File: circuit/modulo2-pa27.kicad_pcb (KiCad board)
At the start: 2 copper layers, 105 x 47 mm, 48 parts, among them J1 CONN_01X02, J3 CONN_01X04, J4 JACK_MONO, J5 HOLE, J7 HOLE, SW1 bright, U1 OPA2134, U2 OPA2134, U3 TLE2426, U4 POWER

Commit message: getting closer to the final PCBs; still have to change the rotenc
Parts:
- moved J1 4.00 mm to (85.0, 93.0)
- moved J3 2.00 mm to (74.0, 93.0)
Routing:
- net /PA_OUT: track 30.2 -> 26.0 mm
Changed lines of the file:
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@@
   (net 33 "/MID")
   (footprint "myAmp:PIN_1x04" (layer "F.Cu")
-    (at 76 93)
+    (at 74 93)
     (property "Sheetfile" "modulo2-pa27.kicad_sch")
     (property "Sheetname" "")
@@
   )
   (footprint "myAmp:PIN_1x02" (layer "F.Cu")
-    (at 89 93)
+    (at 85 93)
     (property "Sheetfile" "modulo2-pa27.kicad_sch")
     (property "Sheetname" "")
@@
   (segment (start 89.0524 80.645) (end 90.805 80.645) (width 0.9144) (layer "F.Cu") (net 13))
   (segment (start 82.55 83.185) (end 81.915 83.82) (width 0.9144) (layer "F.Cu") (net 13))
-  (segment (start 90.27 93) (end 90.27 91.54) (width 0.9144) (layer "F.Cu") (net 14))
-  (segment (start 79.81 90.605) (end 79.7306 90.5256) (width 0.9144) (layer "F.Cu") (net 14))
-  (segment (start 77.8764 90.5256) (end 74.6506 90.5256) (width 0.9144) (layer "F.Cu") (net 14))
-  (segment (start 74.73 93) (end 74.73 90.605) (width 0.9144) (layer "F.Cu") (net 14))
-  (segment (start 79.81 93) (end 79.81 90.605) (width 0.9144) (layer "F.Cu") (net 14))
-  (segment (start 79.7306 90.5256) (end 77.8764 90.5256) (width 0.9144) (layer "F.Cu") (net 14))
   (segment (start 70.2056 90.5256) (end 67.945 88.265) (width 0.9144) (layer "F.Cu") (net 14))
-  (segment (start 89.2556 90.5256) (end 79.7306 90.5256) (width 0.9144) (layer "F.Cu") (net 14))
-  (segment (start 74.6506 90.5256) (end 70.2056 90.5256) (width 0.9144) (layer "F.Cu") (net 14))
-  (segment (start 74.73 90.605) (end 74.6506 90.5256) (width 0.9144) (layer "F.Cu") (net 14))
-  (segment (start 90.27 91.54) (end 89.2556 90.5256) (width 0.9144) (layer "F.Cu") (net 14))
+  (segment (start 77.81 90.5412) (end 77.8256 90.5256) (width 0.9144) (layer "F.Cu") (net 14))
+  (segment (start 86.27 93) (end 86.27 91.731) (width 0.9144) (layer "F.Cu") (net 14))
+  (segment (start 72.7456 90.5256) (end 77.8256 90.5256) (width 0.9144) (layer "F.Cu") (net 14))
+  (segment (start 72.73 93) (end 72.73 90.5412) (width 0.9144) (layer "F.Cu") (net 14))
+  (segment (start 77.81 93) (end 77.81 90.5412) (width 0.9144) (layer "F.Cu") (net 14))
+  (segment (start 77.8256 90.5256) (end 85.0646 90.5256) (width 0.9144) (layer "F.Cu") (net 14))
+  (segment (start 86.27 91.731) (end 85.0646 90.5256) (width 0.9144) (layer "F.Cu") (net 14))
+  (segment (start 72.73 90.5412) (end 72.7456 90.5256) (width 0.9144) (layer "F.Cu") (net 14))
+  (segment (start 70.2056 90.5256) (end 72.7456 90.5256) (width 0.9144) (layer "F.Cu") (net 14))
   (segment (start 77.47 58.42) (end 77.47 60.325) (width 0.9144) (layer "F.Cu") (net 15))
   (segment (start 102.87 60.92) (end 107.315 60.92) (width 0.9144) (layer "F.Cu") (net 16))

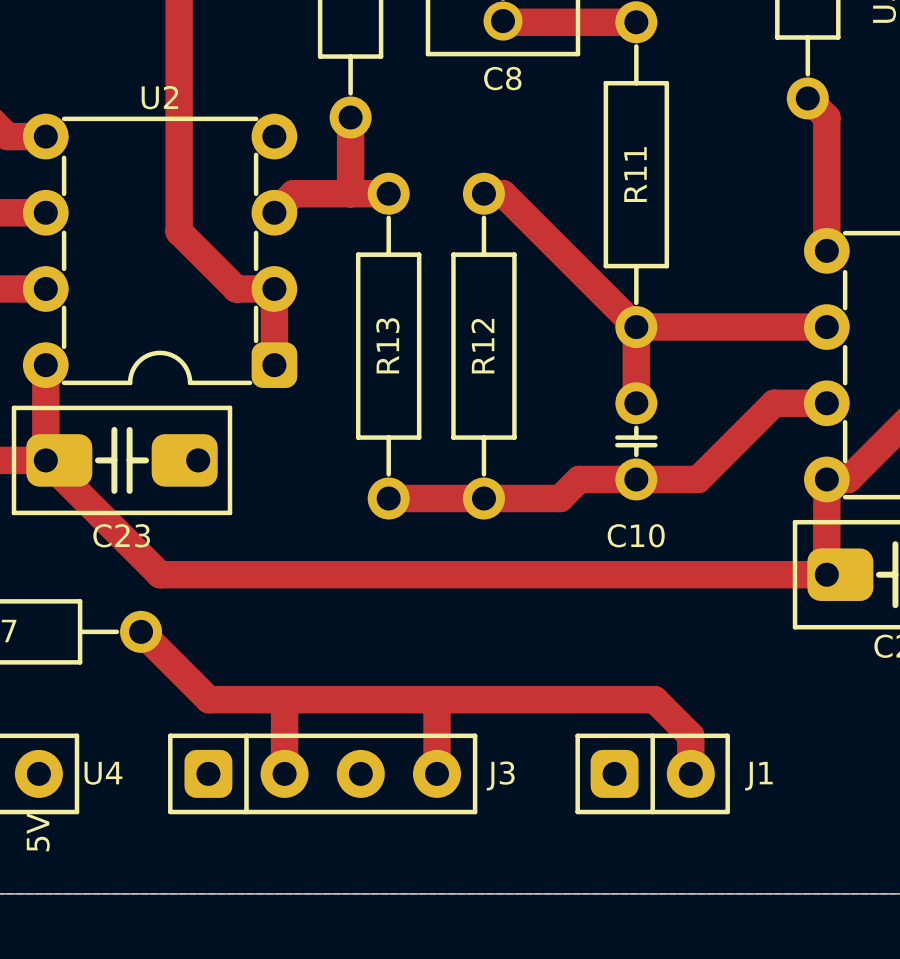
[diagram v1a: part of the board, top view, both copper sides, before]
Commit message: found new switch for gain select; eq needs redesign
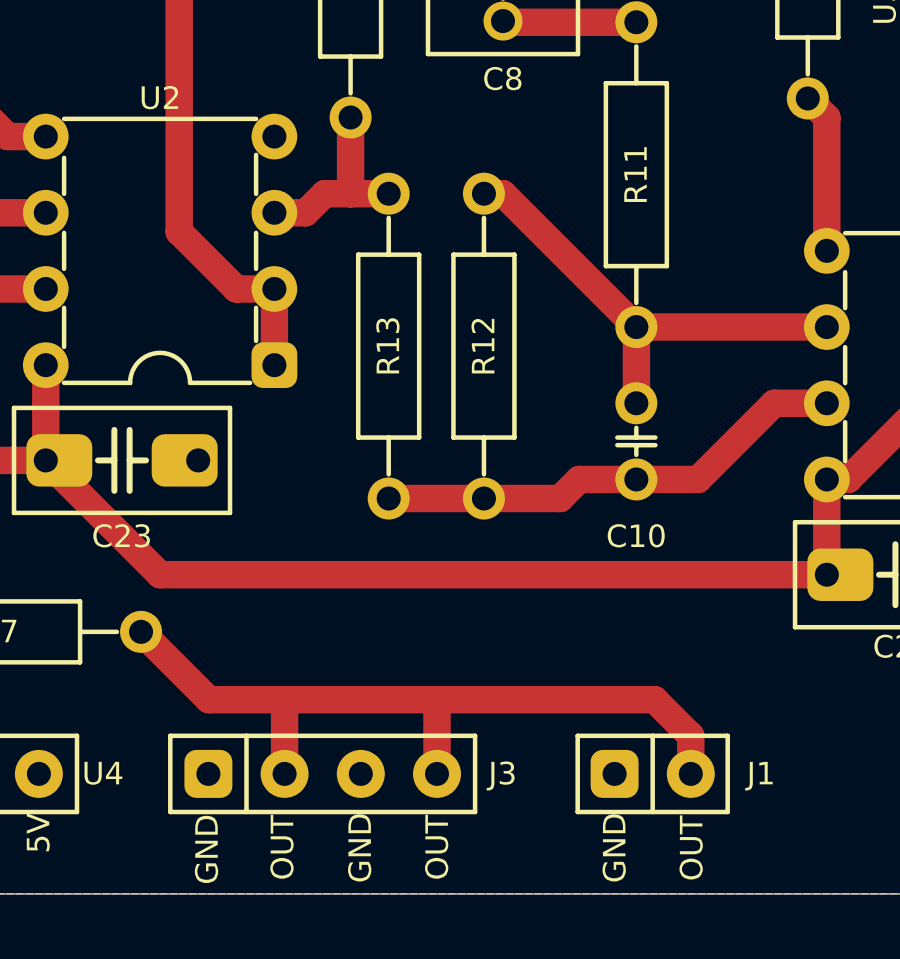
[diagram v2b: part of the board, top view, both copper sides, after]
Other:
- board text added: "GND"
- board text added: "OUT"
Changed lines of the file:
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@@
   (gr_line (start 51 50) (end 154 50) (layer "Edge.Cuts") (width 0.05))
   (gr_arc (start 155 93) (mid 153.828427 95.828427) (end 151 97) (layer "Edge.Cuts") (width 0.05))
+  (gr_text "GND" (at 70.1548 94.3356 90) (layer "F.SilkS")
+    (effects (font (size 0.75 0.75) (thickness 0.15)) (justify right))
+  )
   (gr_text "2022/03/06" (at 110.49 93.98) (layer "F.SilkS")
     (effects (font (size 2 2) (thickness 0.3)))
   )
+  (gr_text "GND" (at 83.7438 94.2848 90) (layer "F.SilkS")
+    (effects (font (size 0.75 0.75) (thickness 0.15)) (justify right))
+  )
+  (gr_text "OUT" (at 86.3092 94.3864 90) (layer "F.SilkS")
+    (effects (font (size 0.75 0.75) (thickness 0.15)) (justify right))
+  )
+  (gr_text "OUT" (at 77.8256 94.361 90) (layer "F.SilkS")
+    (effects (font (size 0.75 0.75) (thickness 0.15)) (justify right))
+  )
   (gr_text "modulo2-pa27" (at 135.255 93.98) (layer "F.SilkS")
     (effects (font (size 2 2) (thickness 0.3)))
+  )
+  (gr_text "GND" (at 75.2602 94.2848 90) (layer "F.SilkS")
+    (effects (font (size 0.75 0.75) (thickness 0.15)) (justify right))
+  )
+  (gr_text "OUT" (at 72.6694 94.361 90) (layer "F.SilkS")
+    (effects (font (size 0.75 0.75) (thickness 0.15)) (justify right))
   )
   (segment (start 94.2086 70.8914) (end 94.2086 80.4926) (width 0.9144) (layer "F.Cu") (net 1))
@@
   (segment (start 90.805 71.12) (end 90.17 70.485) (width 0.9144) (layer "F.Cu") (net 24))
   (segment (start 74.93 71.12) (end 74.93 73.66) (width 0.9144) (layer "F.Cu") (net 25))
-  (segment (start 73.025 73.66) (end 72.39 74.295) (width 0.9144) (layer "F.Cu") (net 25))
-  (segment (start 74.93 73.66) (end 73.025 73.66) (width 0.9144) (layer "F.Cu") (net 25))
+  (segment (start 73.4314 74.295) (end 72.39 74.295) (width 0.9144) (layer "F.Cu") (net 25))
+  (segment (start 74.93 73.66) (end 74.0664 73.66) (width 0.9144) (layer "F.Cu") (net 25))
+  (segment (start 74.0664 73.66) (end 73.4314 74.295) (width 0.9144) (layer "F.Cu") (net 25))
   (segment (start 76.2 73.66) (end 74.93 73.66) (width 0.9144) (layer "F.Cu") (net 25))
   (segment (start 54.61 85.09) (end 57.785 88.265) (width 0.9144) (layer "F.Cu") (net 26))
